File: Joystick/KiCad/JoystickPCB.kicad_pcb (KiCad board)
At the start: 2 copper layers, 62 x 42 mm, 20 parts, among them J1 JST B6B-PH-SM4-TB, J2 JST B4B-PH-SM4-TB, J3 JST B4B-PH-SM4-TB, J4 JST B3B-PH-SM4-TB, U1 MIC5225-1.8YM5-TR, U2 ADS1115IDGSR, U3 ICM-20948

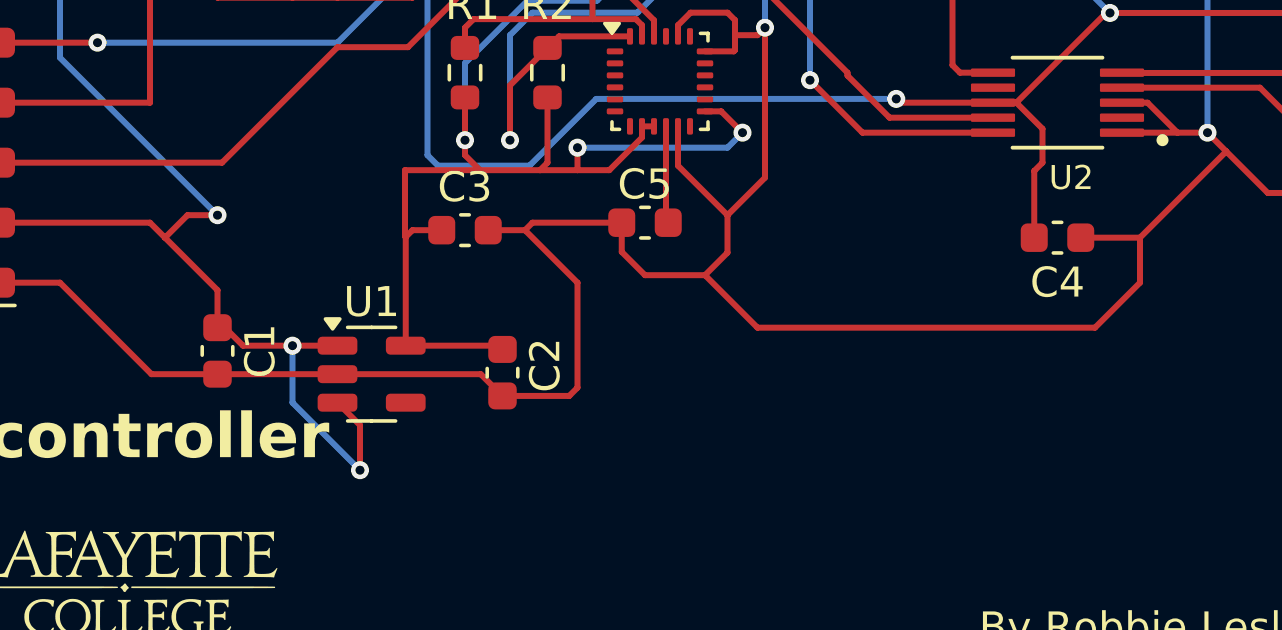
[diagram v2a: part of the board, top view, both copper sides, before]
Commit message: Switch 10uF cap sizes
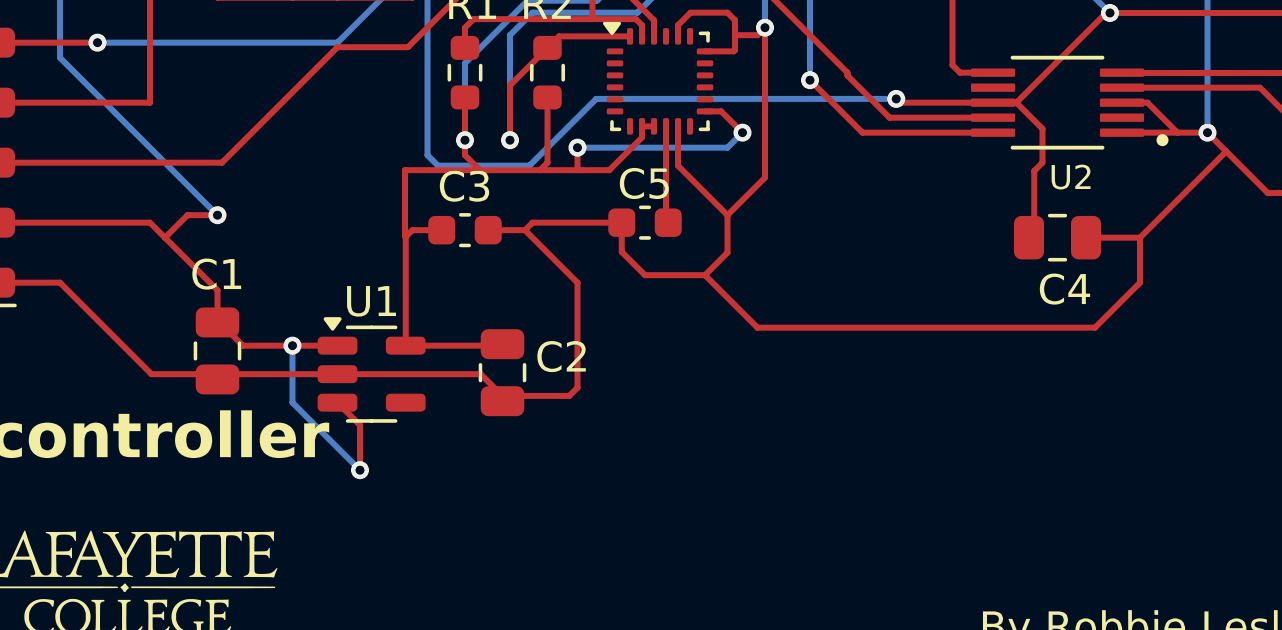
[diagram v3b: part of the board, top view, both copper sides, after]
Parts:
- C1, C2, C4: footprint Capacitor_SMD:C_0603_1608Metric -> Capacitor_SMD:C_0805_2012Metric
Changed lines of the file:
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@@
 		)
 	)
-	(footprint "Capacitor_SMD:C_0603_1608Metric"
+	(footprint "Capacitor_SMD:C_0805_2012Metric"
 		(layer "F.Cu")
 		(at 170 71.5)
-		(descr "Capacitor SMD 0603 (1608 Metric), square (rectangular) end terminal, IPC_7351 nominal, (Body size source: IPC-SM-782 page 76, https://www.pcb-3d.com/wordpress/wp-content/uploads/ipc-sm-782a_amendment_1_and_2.pdf), generated with kicad-footprint-generator")
+		(descr "Capacitor SMD 0805 (2012 Metric), square (rectangular) end terminal, IPC_7351 nominal, (Body size source: IPC-SM-782 page 76, https://www.pcb-3d.com/wordpress/wp-content/uploads/ipc-sm-782a_amendment_1_and_2.pdf, https://docs.google.com/spreadsheets/d/1BsfQQcO9C6DZCsRaXUlFlo91Tg2WpOkGARC1WS5S8t0/edit?usp=sharing), generated with kicad-footprint-generator")
 		(tags "capacitor")
 		(property "Reference" "C4"
-			(at 0 1.5 0)
+			(at 0.25 1.75 0)
 			(layer "F.SilkS")
 			(effects
@@
 		)
 		(property "Value" "10uF"
-			(at 0 1.43 0)
+			(at 0 1.68 0)
 			(layer "F.Fab")
 			(effects
@@
 			)
 		)
-		(property "Footprint" "Capacitor_SMD:C_0603_1608Metric"
+		(property "Footprint" "Capacitor_SMD:C_0805_2012Metric"
 			(at 0 0 0)
 			(unlocked yes)
@@
 		(attr smd)
 		(fp_line
-			(start -0.14058 -0.51)
-			(end 0.14058 -0.51)
+			(start -0.261252 -0.735)
+			(end 0.261252 -0.735)
 			(stroke
 				(width 0.12)
@@
 		)
 		(fp_line
-			(start -0.14058 0.51)
-			(end 0.14058 0.51)
+			(start -0.261252 0.735)
+			(end 0.261252 0.735)
 			(stroke
 				(width 0.12)
@@
 		)
 		(fp_line
-			(start -1.48 -0.73)
-			(end 1.48 -0.73)
+			(start -1.7 -0.98)
+			(end 1.7 -0.98)
 			(stroke
 				(width 0.05)
@@
 		)
 		(fp_line
-			(start -1.48 0.73)
-			(end -1.48 -0.73)
+			(start -1.7 0.98)
+			(end -1.7 -0.98)
 			(stroke
 				(width 0.05)
@@
 		)
 		(fp_line
-			(start 1.48 -0.73)
-			(end 1.48 0.73)
+			(start 1.7 -0.98)
+			(end 1.7 0.98)
 			(stroke
 				(width 0.05)
@@
 		)
 		(fp_line
-			(start 1.48 0.73)
-			(end -1.48 0.73)
+			(start 1.7 0.98)
+			(end -1.7 0.98)
 			(stroke
 				(width 0.05)
@@
 		)
 		(fp_line
-			(start -0.8 -0.4)
-			(end 0.8 -0.4)
+			(start -1 -0.625)
+			(end 1 -0.625)
 			(stroke
 				(width 0.1)
@@
 		)
 		(fp_line
-			(start -0.8 0.4)
-			(end -0.8 -0.4)
+			(start -1 0.625)
+			(end -1 -0.625)
 			(stroke
 				(width 0.1)
@@
 		)
 		(fp_line
-			(start 0.8 -0.4)
-			(end 0.8 0.4)
+			(start 1 -0.625)
+			(end 1 0.625)
 			(stroke
 				(width 0.1)
@@
 		)
 		(fp_line
-			(start 0.8 0.4)
-			(end -0.8 0.4)
+			(start 1 0.625)
+			(end -1 0.625)
 			(stroke
 				(width 0.1)
@@
 			(effects
 				(font
-					(size 0.4 0.4)
-					(thickness 0.06)
+					(size 0.5 0.5)
+					(thickness 0.08)
 				)
 			)
 		)
 		(pad "1" smd roundrect
-			(at -0.775 0)
-			(size 0.9 0.95)
+			(at -0.95 0)
+			(size 1 1.45)
 			(layers "F.Cu" "F.Paste" "F.Mask")
 			(roundrect_rratio 0.25)
@@
 		)
 		(pad "2" smd roundrect
-			(at 0.775 0)
-			(size 0.9 0.95)
+			(at 0.95 0)
+			(size 1 1.45)
 			(layers "F.Cu" "F.Paste" "F.Mask")
 			(roundrect_rratio 0.25)
@@
 			(pintype "passive")
 		)
-		(model "${KICAD8_3DMODEL_DIR}/Capacitor_SMD.3dshapes/C_0603_1608Metric.wrl"
+		(model "${KICAD8_3DMODEL_DIR}/Capacitor_SMD.3dshapes/C_0805_2012Metric.wrl"
 			(offset
 				(xyz 0 0 0)
@@
 		)
 	)
-	(footprint "Capacitor_SMD:C_0603_1608Metric"
+	(footprint "Capacitor_SMD:C_0805_2012Metric"
 		(layer "F.Cu")
 		(at 151.5 76 -90)
-		(descr "Capacitor SMD 0603 (1608 Metric), square (rectangular) end terminal, IPC_7351 nominal, (Body size source: IPC-SM-782 page 76, https://www.pcb-3d.com/wordpress/wp-content/uploads/ipc-sm-782a_amendment_1_and_2.pdf), generated with kicad-footprint-generator")
+		(descr "Capacitor SMD 0805 (2012 Metric), square (rectangular) end terminal, IPC_7351 nominal, (Body size source: IPC-SM-782 page 76, https://www.pcb-3d.com/wordpress/wp-content/uploads/ipc-sm-782a_amendment_1_and_2.pdf, https://docs.google.com/spreadsheets/d/1BsfQQcO9C6DZCsRaXUlFlo91Tg2WpOkGARC1WS5S8t0/edit?usp=sharing), generated with kicad-footprint-generator")
 		(tags "capacitor")
 		(property "Reference" "C2"
-			(at -0.25 -1.43 90)
+			(at -0.5 -2 0)
 			(layer "F.SilkS")
 			(effects
@@
 		)
 		(property "Value" "10uF"
-			(at 0 1.43 90)
+			(at 0 1.68 -90)
 			(layer "F.Fab")
 			(effects
@@
 			)
 		)
-		(property "Footprint" "Capacitor_SMD:C_0603_1608Metric"
+		(property "Footprint" "Capacitor_SMD:C_0805_2012Metric"
 			(at 0 0 -90)
 			(unlocked yes)
@@
 		(attr smd)
 		(fp_line
-			(start -0.14058 0.51)
-			(end 0.14058 0.51)
+			(start -0.261252 0.735)
+			(end 0.261252 0.735)
 			(stroke
 				(width 0.12)
@@
 		)
 		(fp_line
-			(start -0.14058 -0.51)
-			(end 0.14058 -0.51)
+			(start -0.261252 -0.735)
+			(end 0.261252 -0.735)
 			(stroke
 				(width 0.12)
@@
 		)
 		(fp_line
-			(start -1.48 0.73)
-			(end -1.48 -0.73)
+			(start -1.7 0.98)
+			(end -1.7 -0.98)
 			(stroke
 				(width 0.05)
@@
 		)
 		(fp_line
-			(start 1.48 0.73)
-			(end -1.48 0.73)
+			(start 1.7 0.98)
+			(end -1.7 0.98)
 			(stroke
 				(width 0.05)
@@
 		)
 		(fp_line
-			(start -1.48 -0.73)
-			(end 1.48 -0.73)
+			(start -1.7 -0.98)
+			(end 1.7 -0.98)
 			(stroke
 				(width 0.05)
@@
 		)
 		(fp_line
-			(start 1.48 -0.73)
-			(end 1.48 0.73)
+			(start 1.7 -0.98)
+			(end 1.7 0.98)
 			(stroke
 				(width 0.05)
@@
 		)
 		(fp_line
-			(start -0.8 0.4)
-			(end -0.8 -0.4)
+			(start -1 0.625)
+			(end -1 -0.625)
 			(stroke
 				(width 0.1)
@@
 		)
 		(fp_line
-			(start 0.8 0.4)
-			(end -0.8 0.4)
+			(start 1 0.625)
+			(end -1 0.625)
 			(stroke
 				(width 0.1)
@@
 		)
 		(fp_line
-			(start -0.8 -0.4)
-			(end 0.8 -0.4)
+			(start -1 -0.625)
+			(end 1 -0.625)
 			(stroke
 				(width 0.1)
@@
 		)
 		(fp_line
-			(start 0.8 -0.4)
-			(end 0.8 0.4)
+			(start 1 -0.625)
+			(end 1 0.625)
 			(stroke
 				(width 0.1)
@@
 		)
 		(fp_text user "${REFERENCE}"
-			(at 0 0 90)
+			(at 0 0 -90)
 			(layer "F.Fab")
 			(effects
 				(font
-					(size 0.4 0.4)
-					(thickness 0.06)
+					(size 0.5 0.5)
+					(thickness 0.08)
 				)
 			)
 		)
 		(pad "1" smd roundrect
-			(at -0.775 0 270)
-			(size 0.9 0.95)
+			(at -0.95 0 270)
+			(size 1 1.45)
 			(layers "F.Cu" "F.Paste" "F.Mask")
 			(roundrect_rratio 0.25)
@@
 		)
 		(pad "2" smd roundrect
-			(at 0.775 0 270)
-			(size 0.9 0.95)
+			(at 0.95 0 270)
+			(size 1 1.45)
 			(layers "F.Cu" "F.Paste" "F.Mask")
 			(roundrect_rratio 0.25)
@@
 			(pintype "passive")
 		)
-		(model "${KICAD8_3DMODEL_DIR}/Capacitor_SMD.3dshapes/C_0603_1608Metric.wrl"
+		(model "${KICAD8_3DMODEL_DIR}/Capacitor_SMD.3dshapes/C_0805_2012Metric.wrl"
 			(offset
 				(xyz 0 0 0)
@@
 		)
 	)
-	(footprint "Capacitor_SMD:C_0603_1608Metric"
+	(footprint "Capacitor_SMD:C_0805_2012Metric"
 		(layer "F.Cu")
 		(at 142 75.275 -90)
-		(descr "Capacitor SMD 0603 (1608 Metric), square (rectangular) end terminal, IPC_7351 nominal, (Body size source: IPC-SM-782 page 76, https://www.pcb-3d.com/wordpress/wp-content/uploads/ipc-sm-782a_amendment_1_and_2.pdf), generated with kicad-footprint-generator")
+		(descr "Capacitor SMD 0805 (2012 Metric), square (rectangular) end terminal, IPC_7351 nominal, (Body size source: IPC-SM-782 page 76, https://www.pcb-3d.com/wordpress/wp-content/uploads/ipc-sm-782a_amendment_1_and_2.pdf, https://docs.google.com/spreadsheets/d/1BsfQQcO9C6DZCsRaXUlFlo91Tg2WpOkGARC1WS5S8t0/edit?usp=sharing), generated with kicad-footprint-generator")
 		(tags "capacitor")
 		(property "Reference" "C1"
-			(at 0 -1.43 90)
+			(at -2.525 0 0)
 			(layer "F.SilkS")
 			(effects
@@
 		)
 		(property "Value" "10uF"
-			(at 0 1.43 90)
+			(at 0 1.68 -90)
 			(layer "F.Fab")
 			(effects
@@
 			)
 		)
-		(property "Footprint" "Capacitor_SMD:C_0603_1608Metric"
+		(property "Footprint" "Capacitor_SMD:C_0805_2012Metric"
 			(at 0 0 -90)
 			(unlocked yes)
@@
 		(attr smd)
 		(fp_line
-			(start -0.14058 0.51)
-			(end 0.14058 0.51)
+			(start -0.261252 0.735)
+			(end 0.261252 0.735)
 			(stroke
 				(width 0.12)
@@
 		)
 		(fp_line
-			(start -0.14058 -0.51)
-			(end 0.14058 -0.51)
+			(start -0.261252 -0.735)
+			(end 0.261252 -0.735)
 			(stroke
 				(width 0.12)
@@
 		)
 		(fp_line
-			(start -1.48 0.73)
-			(end -1.48 -0.73)
+			(start -1.7 0.98)
+			(end -1.7 -0.98)
 			(stroke
 				(width 0.05)
@@
 		)
 		(fp_line
-			(start 1.48 0.73)
-			(end -1.48 0.73)
+			(start 1.7 0.98)
+			(end -1.7 0.98)
 			(stroke
 				(width 0.05)
@@
 		)
 		(fp_line
-			(start -1.48 -0.73)
-			(end 1.48 -0.73)
+			(start -1.7 -0.98)
+			(end 1.7 -0.98)
 			(stroke
 				(width 0.05)
@@
 		)
 		(fp_line
-			(start 1.48 -0.73)
-			(end 1.48 0.73)
+			(start 1.7 -0.98)
+			(end 1.7 0.98)
 			(stroke
 				(width 0.05)
@@
 		)
 		(fp_line
-			(start -0.8 0.4)
-			(end -0.8 -0.4)
+			(start -1 0.625)
+			(end -1 -0.625)
 			(stroke
 				(width 0.1)
@@
 		)
 		(fp_line
-			(start 0.8 0.4)
-			(end -0.8 0.4)
+			(start 1 0.625)
+			(end -1 0.625)
 			(stroke
 				(width 0.1)
@@
 		)
 		(fp_line
-			(start -0.8 -0.4)
-			(end 0.8 -0.4)
+			(start -1 -0.625)
+			(end 1 -0.625)
 			(stroke
 				(width 0.1)
@@
 		)
 		(fp_line
-			(start 0.8 -0.4)
-			(end 0.8 0.4)
+			(start 1 -0.625)
+			(end 1 0.625)
 			(stroke
 				(width 0.1)
@@
 		)
 		(fp_text user "${REFERENCE}"
-			(at 0 0 90)
+			(at 0 0 -90)
 			(layer "F.Fab")
 			(effects
 				(font
-					(size 0.4 0.4)
-					(thickness 0.06)
+					(size 0.5 0.5)
+					(thickness 0.08)
 				)
 			)
 		)
 		(pad "1" smd roundrect
-			(at -0.775 0 270)
-			(size 0.9 0.95)
+			(at -0.95 0 270)
+			(size 1 1.45)
 			(layers "F.Cu" "F.Paste" "F.Mask")
 			(roundrect_rratio 0.25)
@@
 		)
 		(pad "2" smd roundrect
-			(at 0.775 0 270)
-			(size 0.9 0.95)
+			(at 0.95 0 270)
+			(size 1 1.45)
 			(layers "F.Cu" "F.Paste" "F.Mask")
 			(roundrect_rratio 0.25)
@@
 			(pintype "passive")
 		)
-		(model "${KICAD8_3DMODEL_DIR}/Capacitor_SMD.3dshapes/C_0603_1608Metric.wrl"
+		(model "${KICAD8_3DMODEL_DIR}/Capacitor_SMD.3dshapes/C_0805_2012Metric.wrl"
 			(offset
 				(xyz 0 0 0)

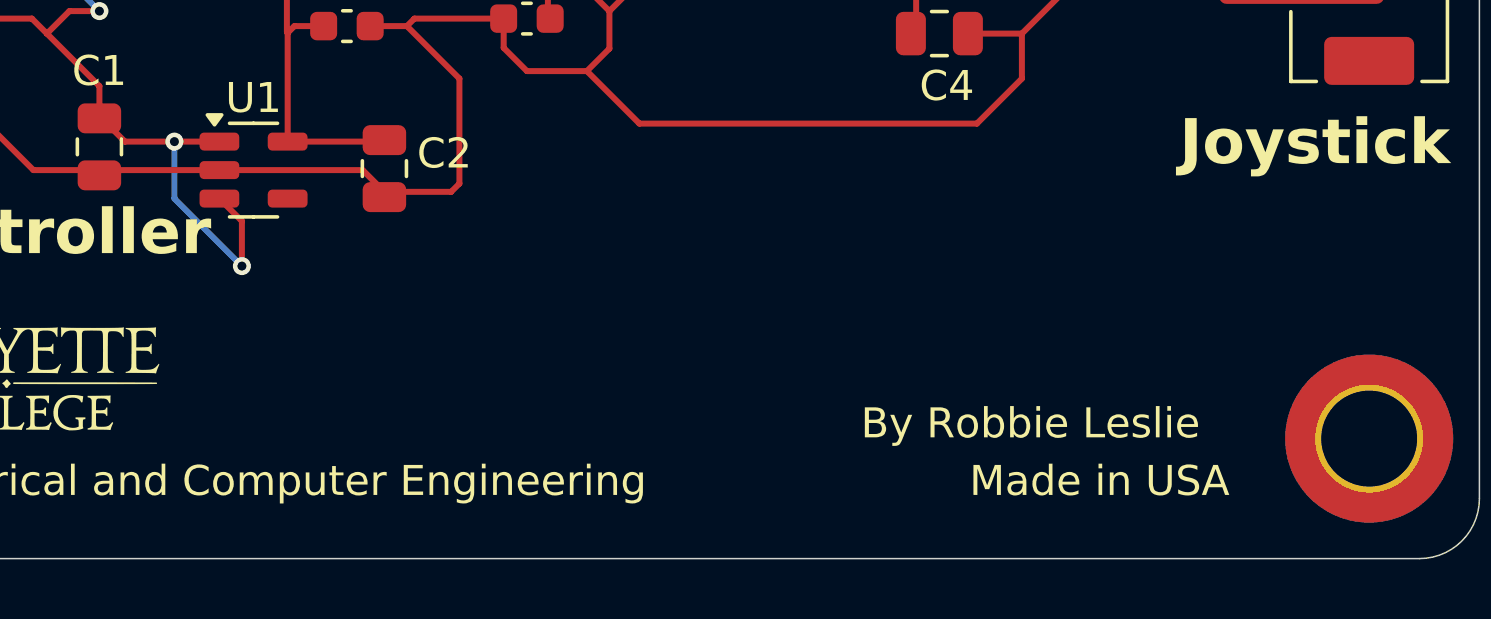
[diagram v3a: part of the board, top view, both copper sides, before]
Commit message: Added required silkscreen components
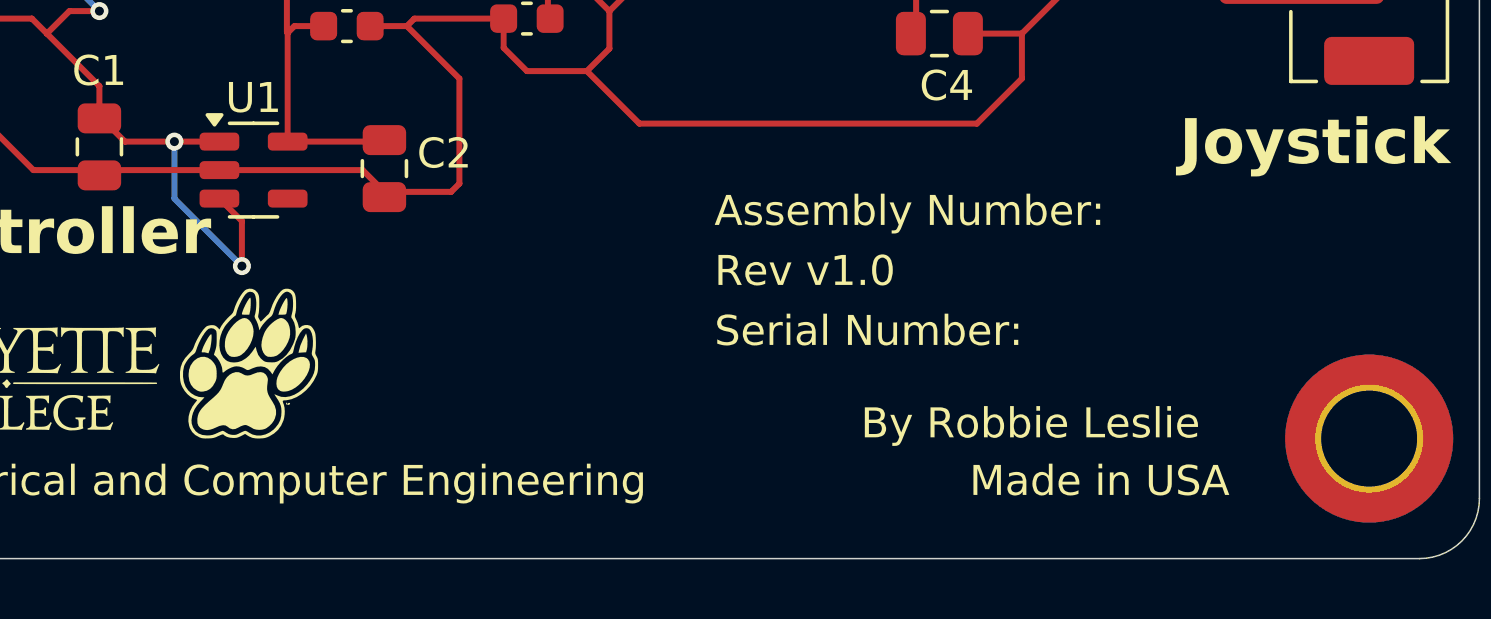
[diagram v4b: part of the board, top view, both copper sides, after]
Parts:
- added G***: LOGO, Footprints:LeopardPawFootprint, F.Cu at (147.0, 82.5)
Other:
- board text added: "1/28/25"
- board text added: "Assembly Number:"
- board text added: "Board Part Number:"
- board text added: "Rev v1.0"
- board text added: "Serial Number:"
- board text removed: "11/9/24"
- board text removed: "Still need to add assembly number and stuff"
